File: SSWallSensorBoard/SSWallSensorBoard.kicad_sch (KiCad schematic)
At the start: 35 parts, among them J1 Conn_01x10

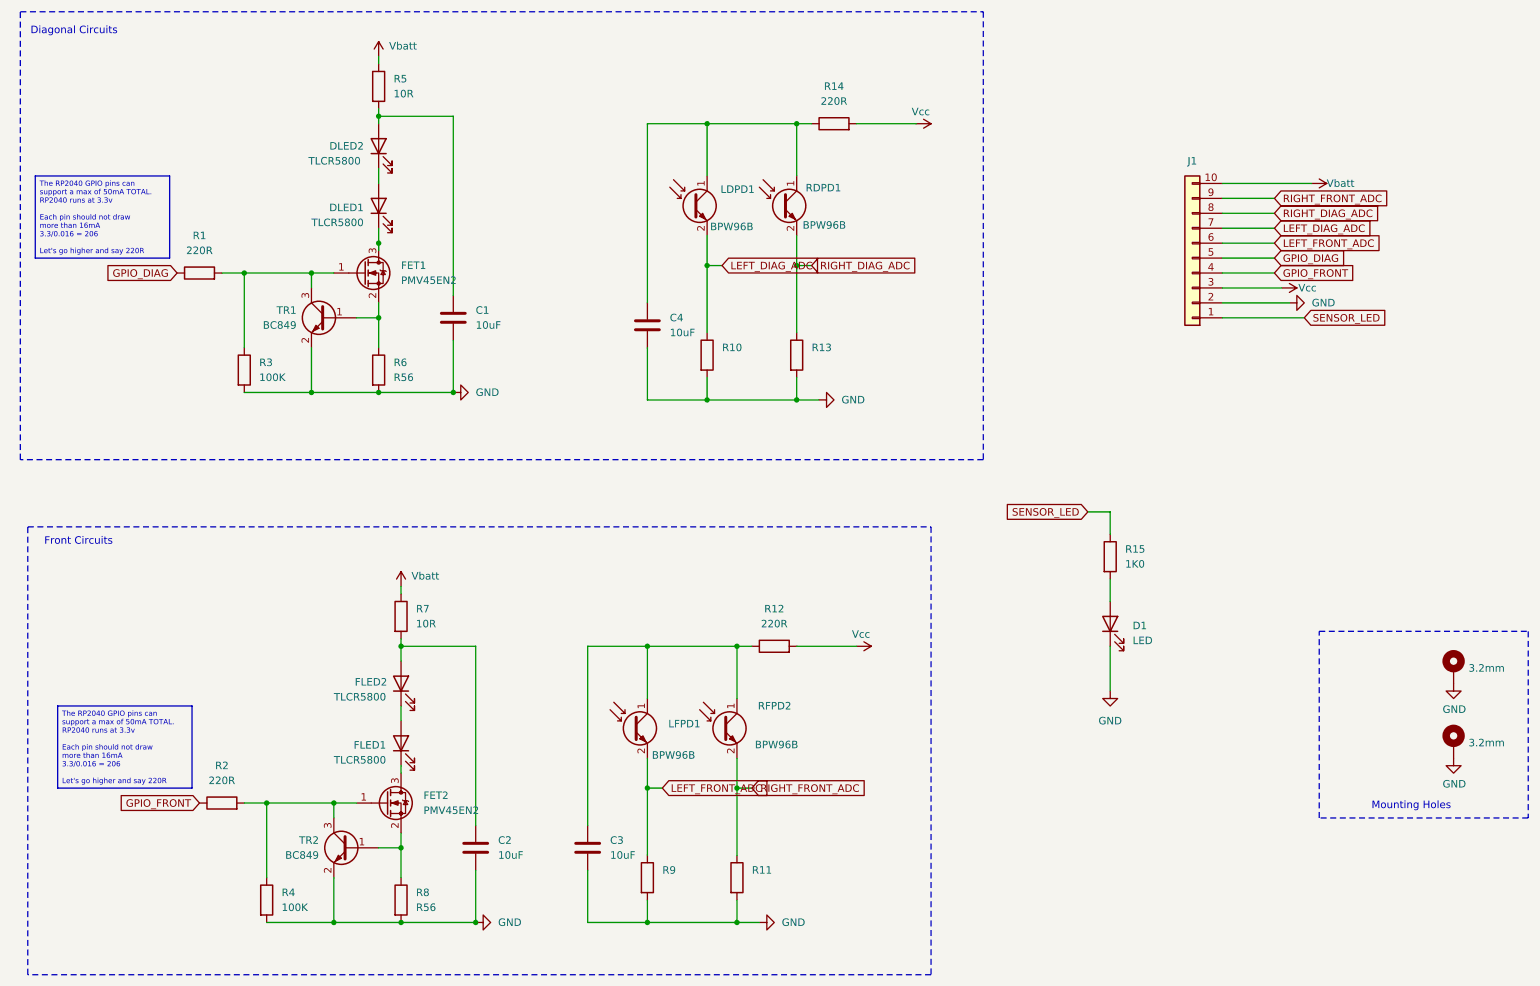
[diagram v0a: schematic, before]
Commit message: Version 2 of boards sent to JLCPCB and a new calibration board
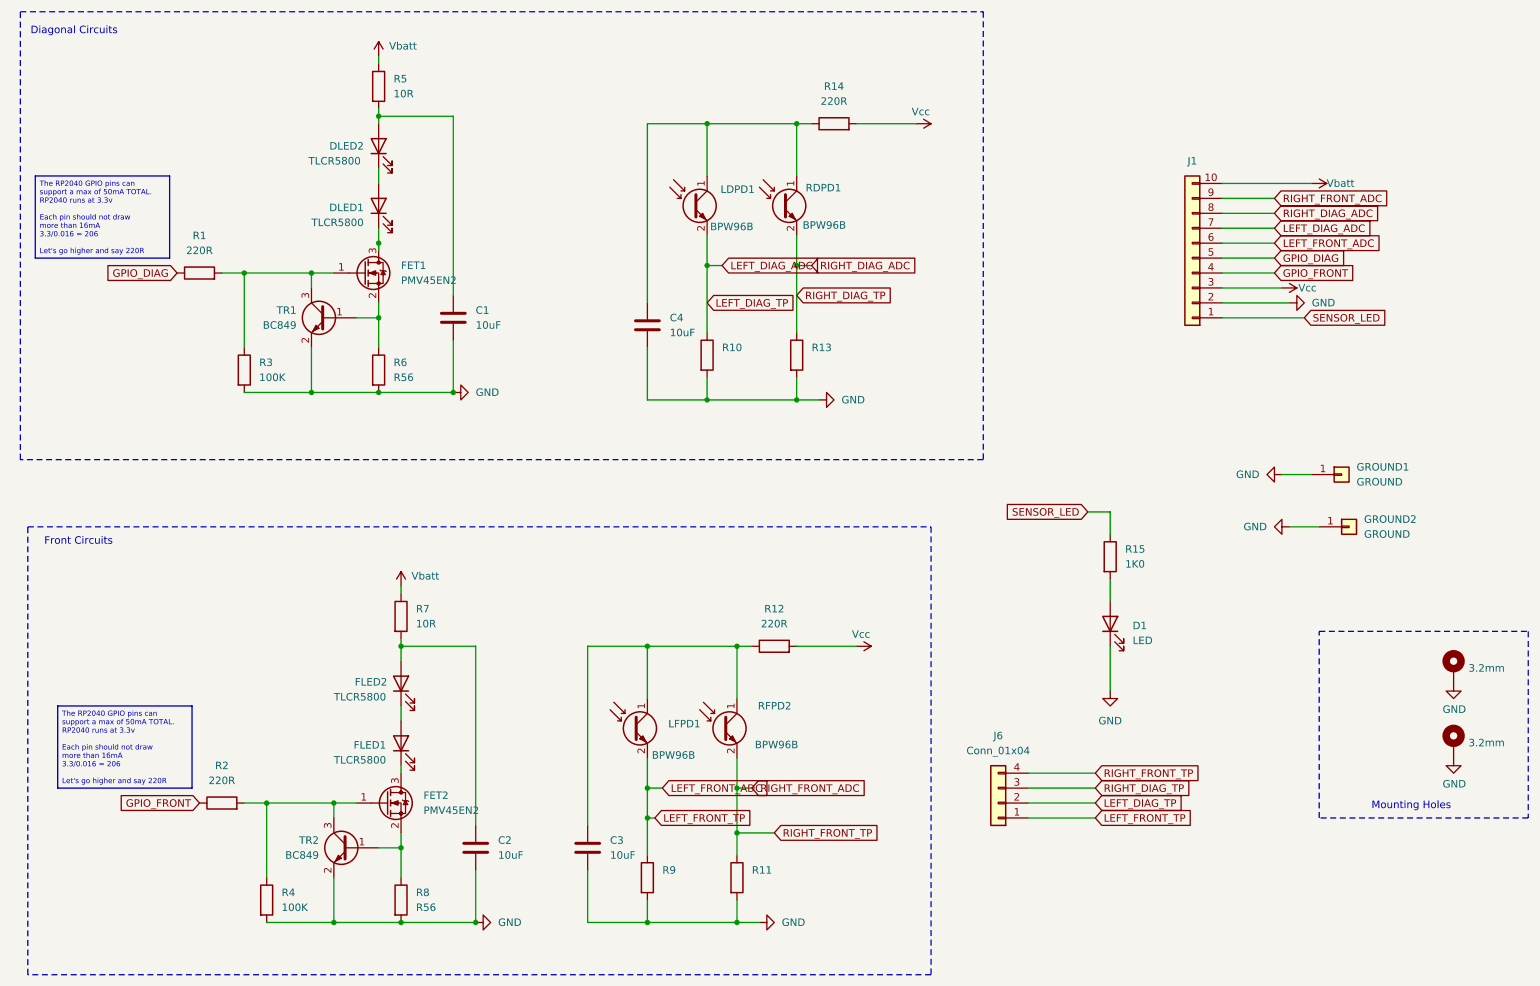
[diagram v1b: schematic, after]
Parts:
- added GROUND1, GROUND2: GROUND, Connector_PinHeader_2.54mm:PinHeader_1x01_P2.54mm_Vertical, symbol Connector_Generic:Conn_01x01
- added J6: Conn_01x04, Connector_PinHeader_2.54mm:PinHeader_1x04_P2.54mm_Vertical, symbol Connector_Generic:Conn_01x04
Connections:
- net GND: now also GROUND1.1 (Pin_1), GROUND2.1 (Pin_1)
- net LEFT_DIAG_ADC: now also J6.2 (Pin_2)
- net LEFT_FRONT_ADC: now also J6.1 (Pin_1)
- net RIGHT_DIAG_ADC: now also J6.3 (Pin_3)
- net RIGHT_FRONT_ADC: now also J6.4 (Pin_4)
